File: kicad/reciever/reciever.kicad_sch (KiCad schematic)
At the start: 10 parts, among them U2 LM2596T-5

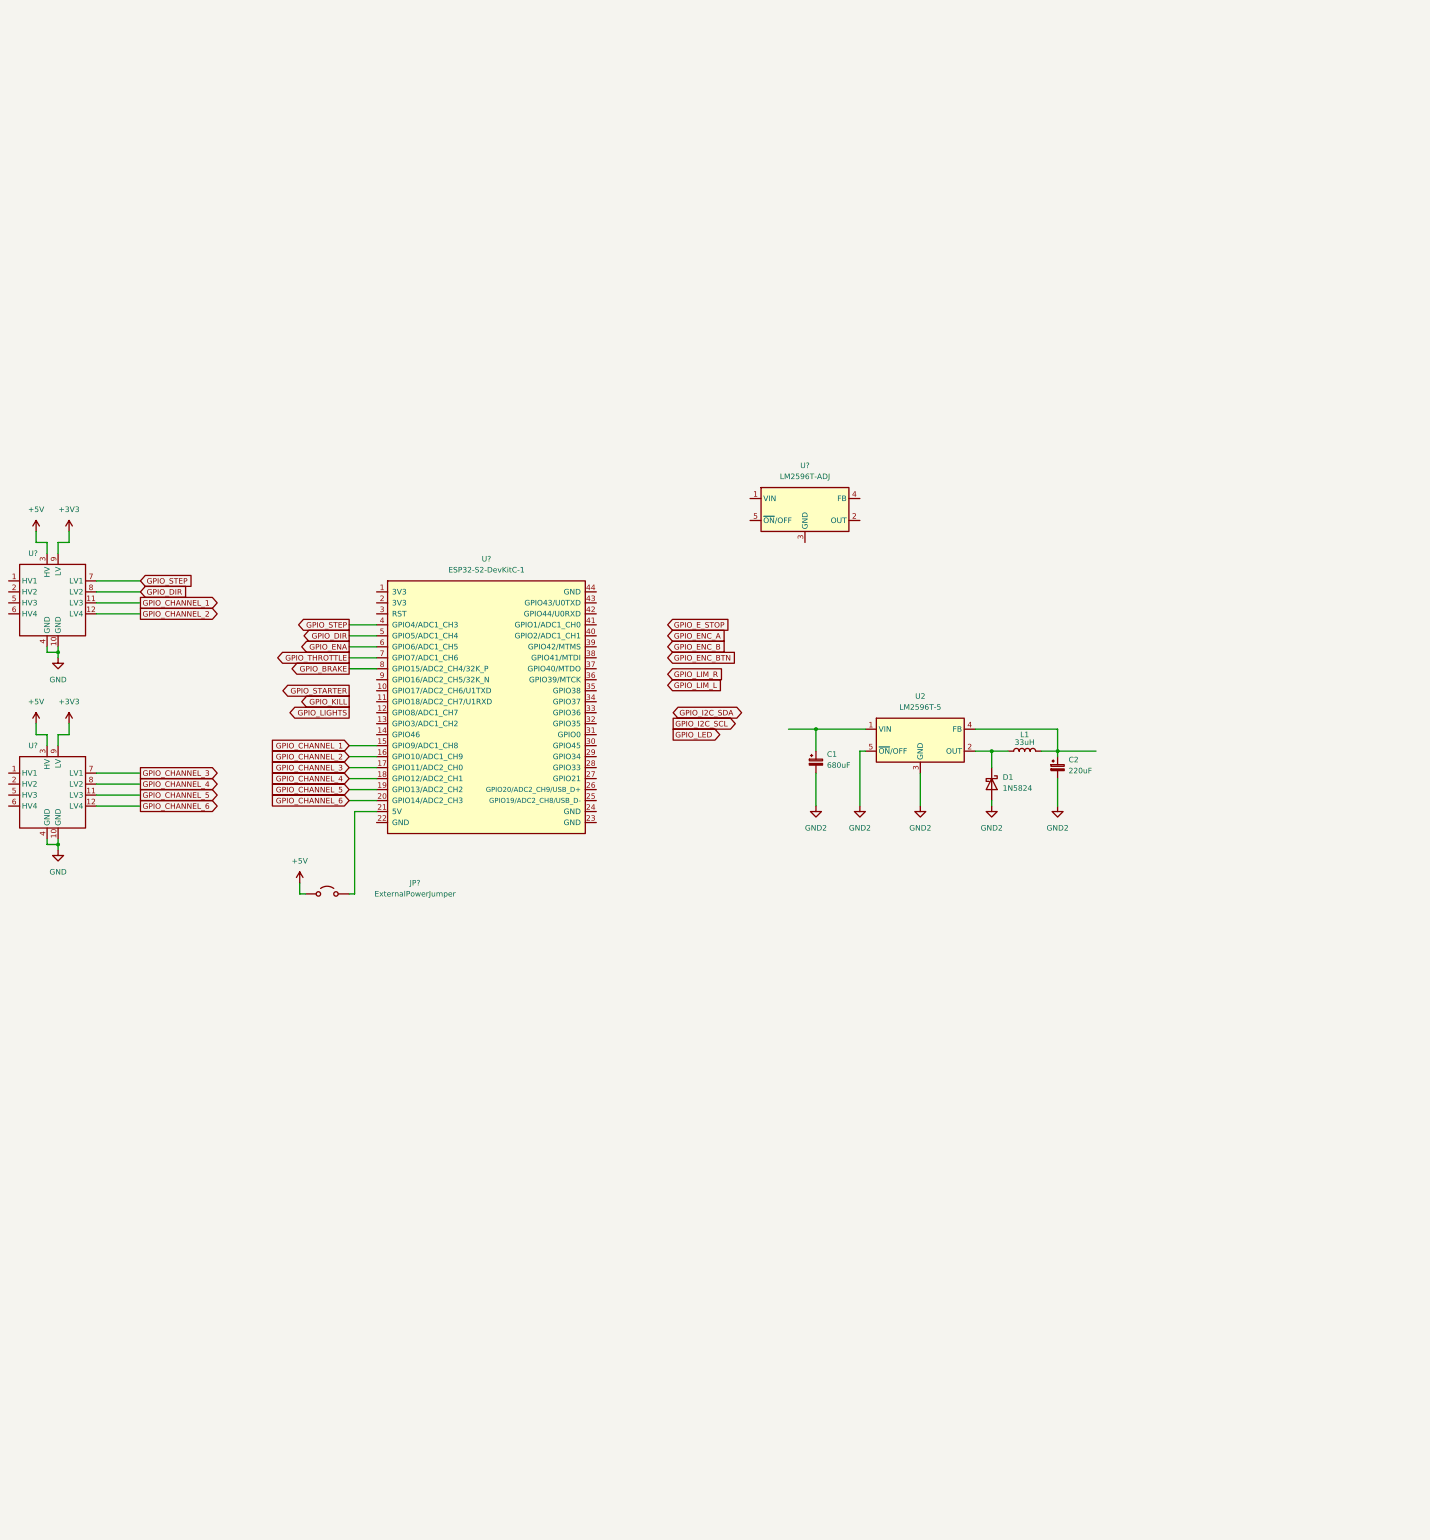
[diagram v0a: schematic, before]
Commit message: throttle servo behaves as expected, brake servo goes all the way and does not come back
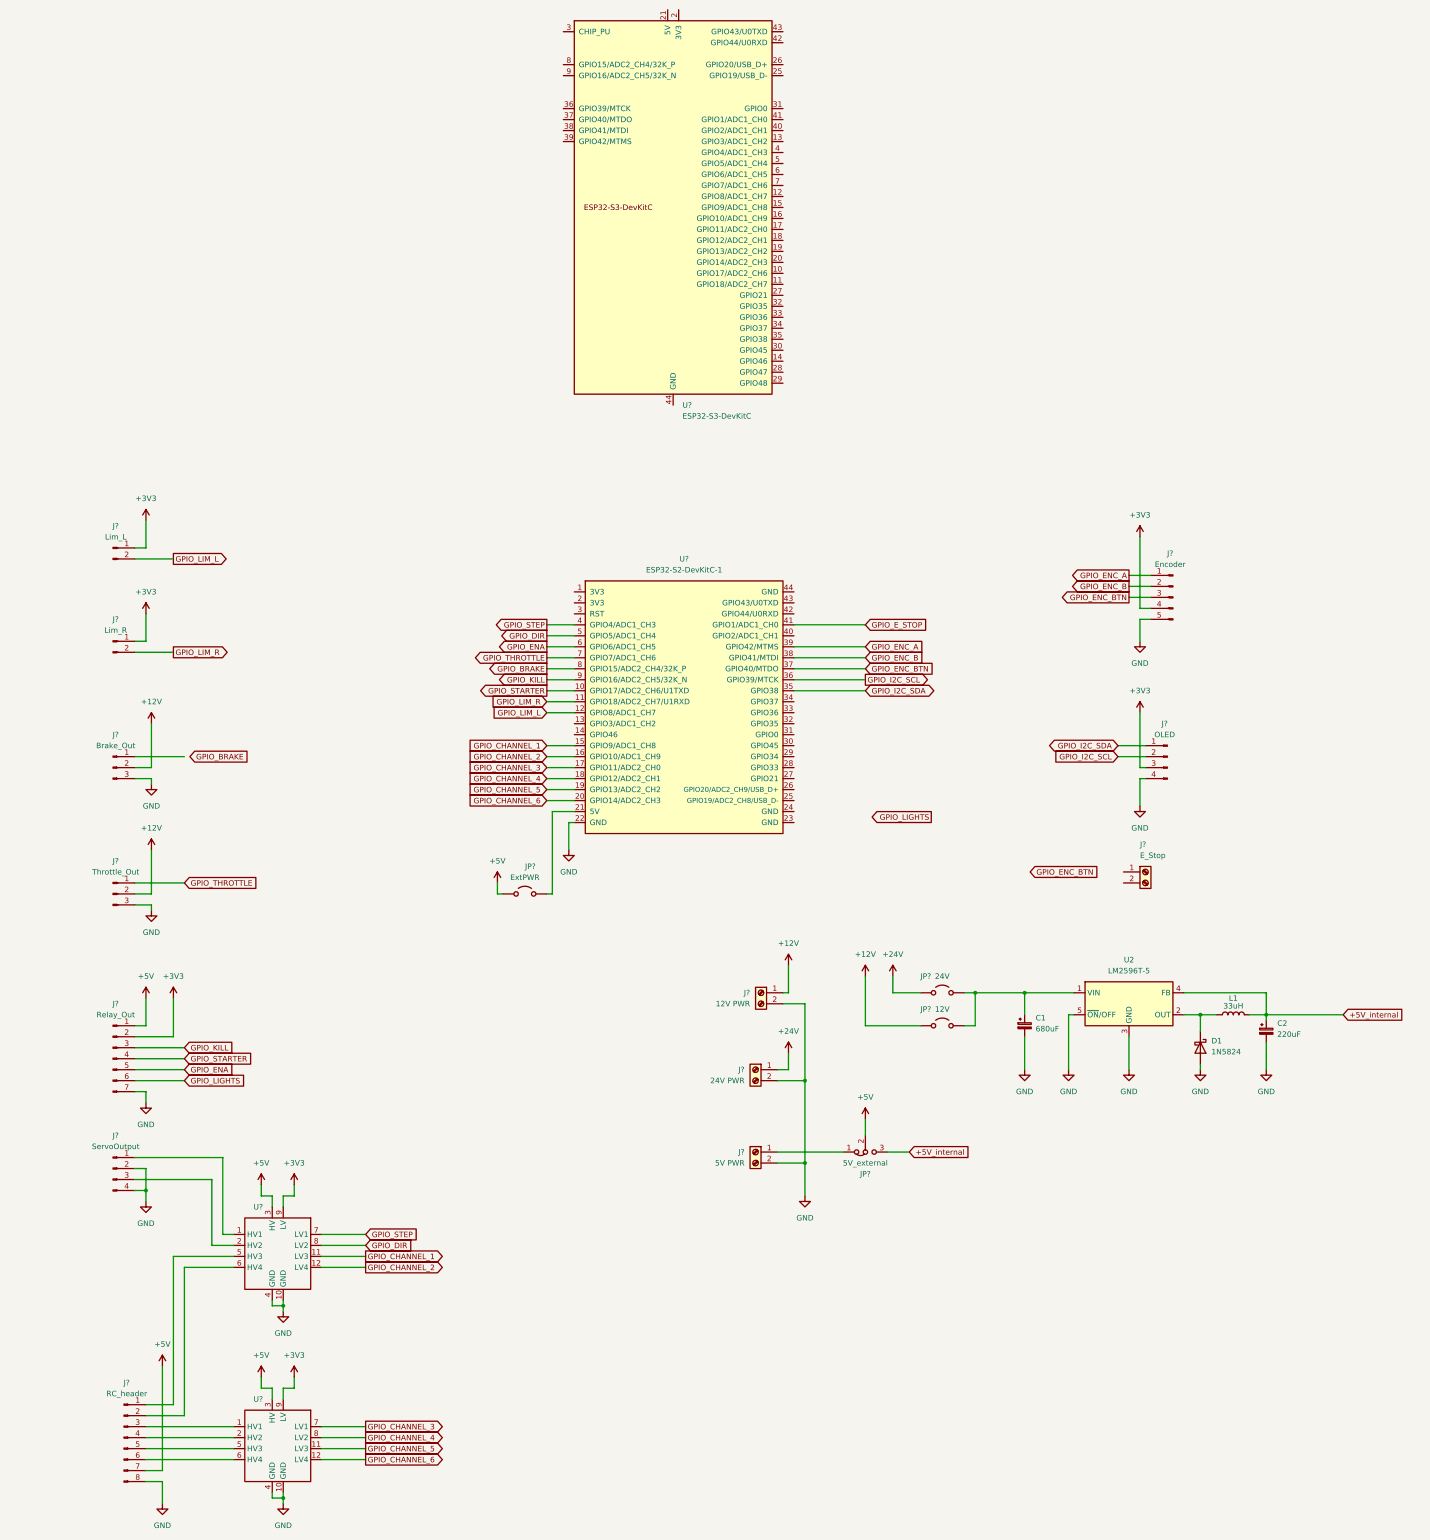
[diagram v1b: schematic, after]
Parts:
- removed U?: LM2596T-ADJ, Package_TO_SOT_THT:TO-220-5_P3.4x3.7mm_StaggerOdd_Lead3.8mm_Vertical, symbol Regulator_Switching:LM2596T-ADJ
- added J?: ServoOutput, symbol Connector:Conn_01x04_Pin
- added J?: 12V PWR, symbol Connector:Screw_Terminal_01x02
- added J?: Throttle_Out, symbol Connector:Conn_01x03_Pin
- added J?: Lim_L, symbol Connector:Conn_01x02_Pin
- added J?: 5V PWR, symbol Connector:Screw_Terminal_01x02
- added J?: Lim_R, symbol Connector:Conn_01x02_Pin
- added J?: Relay_Out, symbol Connector:Conn_01x07_Pin
- added J?: RC_header, symbol Connector:Conn_01x08_Pin
- added J?: Brake_Out, symbol Connector:Conn_01x03_Pin
- added J?: 24V PWR, symbol Connector:Screw_Terminal_01x02
- added J?: Encoder, symbol Connector:Conn_01x05_Pin
- added J?: E_Stop, symbol Connector:Screw_Terminal_01x02
- added J?: OLED, symbol Connector:Conn_01x04_Pin
- added JP?: 5V_external, symbol Jumper:Jumper_3_Bridged12
- added JP?: 24V, symbol Jumper:Jumper_2_Open
- added JP?: 12V, symbol Jumper:Jumper_2_Open
- added U?: ESP32-S3-DevKitC, PCM_Espressif:ESP32-S3-DevKitC, symbol Espressif:ESP32-S3-DevKitC
- JP?: value ExternalPowerJumper -> ExtPWR
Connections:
- net GND2 is gone; now on net GND: C1.2, C2.2, D1.2 (A), U2.3 (GND), U2.5 (~{ON}/OFF)
- net +3V3: now also J?.1 (Pin_1), J?.1 (Pin_1), J?.2 (Pin_2), J?.3 (Pin_3), J?.4 (Pin_4)
- net +5V: now also J?.1 (Pin_1), J?.7 (Pin_7), JP?.2 (C)
- net GND: now also U?.22 (GND), J?.2 (Pin_2), J?.2 (Pin_2), J?.2 (Pin_2), J?.2 (Pin_2), J?.3 (Pin_3), J?.3 (Pin_3), J?.4 (Pin_4), J?.4 (Pin_4), J?.5 (Pin_5), J?.7 (Pin_7), J?.8 (Pin_8)
- net GPIO_ENA: now also J?.5 (Pin_5)
- net GPIO_ENC_A: now also U?.39 (GPIO42/MTMS), J?.1 (Pin_1)
- net GPIO_ENC_B: now also U?.38 (GPIO41/MTDI), J?.2 (Pin_2)
- net GPIO_ENC_BTN: now also U?.37 (GPIO40/MTDO), J?.3 (Pin_3)
- net GPIO_E_STOP: now also U?.41 (GPIO1/ADC1_CH0)
- net GPIO_I2C_SCL: now also U?.36 (GPIO39/MTCK), J?.2 (Pin_2)
- net GPIO_I2C_SDA: now also U?.35 (GPIO38), J?.1 (Pin_1)
- net GPIO_KILL: now also U?.9 (GPIO16/ADC2_CH5/32K_N), J?.3 (Pin_3)
- net GPIO_LIGHTS: now also J?.6 (Pin_6)
- net GPIO_LIM_L: now also U?.12 (GPIO8/ADC1_CH7), J?.2 (Pin_2)
- net GPIO_LIM_R: now also U?.11 (GPIO18/ADC2_CH7/U1RXD), J?.2 (Pin_2)
- net GPIO_STARTER: now also U?.10 (GPIO17/ADC2_CH6/U1TXD), J?.4 (Pin_4)
- net GPIO_THROTTLE: now also J?.1 (Pin_1)
- net at C1.1, U2.1 (VIN): now also JP?.2 (B), JP?.2 (B)
- net +5V_internal: now reaches C2.1, L1.2, U2.4 (FB)
- net +5V_internal: now also JP?.3 (B)
- net at U?.1 (HV1): now also J?.1 (Pin_1)
- net at U?.2 (HV2): now also J?.3 (Pin_3)
- net at U?.5 (HV3): now also J?.1 (Pin_1)
- net at U?.6 (HV4): now also J?.2 (Pin_2)
- net at U?.1 (HV1): now also J?.3 (Pin_3)
- net at U?.2 (HV2): now also J?.4 (Pin_4)
- net at U?.5 (HV3): now also J?.5 (Pin_5)
- net at U?.6 (HV4): now also J?.6 (Pin_6)
- new net: J?.1 (Pin_1), JP?.1 (A)
- new net: U?.1 (3V3), U?.2 (3V3)
- new net: U?.22 (GND), U?.23 (GND), U?.24 (GND), U?.44 (GND)
- new net +12V: J?.1 (Pin_1), J?.2 (Pin_2), J?.2 (Pin_2), JP?.1 (A)
- new net +24V: J?.1 (Pin_1), JP?.1 (A)
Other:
- moved on the sheet: C1, C2, D1, JP?, L1, U2, U?
